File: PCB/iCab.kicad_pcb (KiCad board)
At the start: 2 copper layers, 58 parts, among them J1 Jack-DC, J10 PORT5, J11 V12, J2 Jack-DC, J3 PGM, J4 SERIAL, J5 PORT1, J6 PORT2, J7 OUT, J8 PORT3, J9 PORT4, Q1 IRFZ44, Q2 IRFZ44, Q3 IRFZ44, Q4 IRFZ44, Q5 IRFZ44, SW1 SW_Push, U1 Output, U2 PIC18F2550, U3 Output, Y1 Crystal

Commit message: new pcb
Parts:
- removed REF** (x2): MountingHole_2.2mm_M2, Mounting_Holes:MountingHole_2.2mm_M2
- added C10: 1µ, Capacitors_Tantalum_SMD:CP_Tantalum_Case-A_EIA-3216-18_Reflow, F.Cu at (97.8, 48.3)
- added C11: 10µ, Capacitors_THT:CP_Radial_D5.0mm_P2.00mm, F.Cu at (127.0, 53.3)
- added C12: 10µ, Capacitors_THT:CP_Radial_D5.0mm_P2.00mm, F.Cu at (127.0, 71.1)
- added C13: 10µ, Capacitors_THT:CP_Radial_D5.0mm_P2.00mm, F.Cu at (127.0, 88.9)
- added C14: 10µ, Capacitors_THT:CP_Radial_D5.0mm_P2.00mm, F.Cu at (127.0, 106.7)
- added C7: 10µ, Capacitors_THT:CP_Radial_D5.0mm_P2.00mm, F.Cu at (104.1, 47.0)
- added C8: 1µ, Capacitors_Tantalum_SMD:CP_Tantalum_Case-A_EIA-3216-18_Reflow, F.Cu at (85.1, 43.2)
- added C9: 10µ, Capacitors_THT:CP_Radial_D5.0mm_P2.00mm, F.Cu at (127.0, 35.6)
- added D10: D, Diodes_THT:D_T-1_P10.16mm_Horizontal, F.Cu at (92.7, 38.1)
- added D11: LED, LEDs:LED_0603_HandSoldering, F.Cu at (74.9, 52.7)
- added D12: LED, LEDs:LED_0603_HandSoldering, F.Cu at (74.9, 70.5)
- added D13: LED, LEDs:LED_0603_HandSoldering, F.Cu at (74.9, 88.3)
- added D14: LED, LEDs:LED_0603_HandSoldering, F.Cu at (74.9, 106.0)
- added D15: LED, LEDs:LED_0603_HandSoldering, F.Cu at (82.5, 113.0)
- added D16: LED, LEDs:LED_0603_HandSoldering, F.Cu at (116.8, 41.3)
- added D17: LED, LEDs:LED_0603_HandSoldering, F.Cu at (101.6, 79.4)
- added D18: LED, LEDs:LED_0603_HandSoldering, F.Cu at (116.8, 59.1)
- added D19: LED, LEDs:LED_0603_HandSoldering, F.Cu at (116.8, 76.8)
- added D20: LED, LEDs:LED_0603_HandSoldering, F.Cu at (116.8, 94.6)
- added D21: LED, LEDs:LED_0603_HandSoldering, F.Cu at (116.8, 112.4)
- added D8: D, Diodes_THT:D_T-1_P10.16mm_Horizontal, F.Cu at (114.3, 41.9)
- added D9: D, Diodes_THT:D_T-1_P10.16mm_Horizontal, F.Cu at (82.5, 34.3)
- added G***: LOGO, panda:LOGO3, F.Cu at (107.3, 55.9)
- added J12: D3, TerminalBlock_Phoenix:TerminalBlock_Phoenix_MKDS-1,5-2_1x02_P5.00mm_Horizontal, F.Cu at (128.3, 77.5)
- added J13: D4, TerminalBlock_Phoenix:TerminalBlock_Phoenix_MKDS-1,5-2_1x02_P5.00mm_Horizontal, F.Cu at (128.3, 95.2)
- added J14: D5, TerminalBlock_Phoenix:TerminalBlock_Phoenix_MKDS-1,5-2_1x02_P5.00mm_Horizontal, F.Cu at (128.3, 113.0)
- added R23: 511, Resistors_SMD:R_0603_HandSoldering, F.Cu at (78.1, 52.1)
- added R24: 511, Resistors_SMD:R_0603_HandSoldering, F.Cu at (78.1, 69.8)
- added R25: 511, Resistors_SMD:R_0603_HandSoldering, F.Cu at (78.1, 87.6)
- added R26: 511, Resistors_SMD:R_0603_HandSoldering, F.Cu at (78.1, 105.4)
- added R27: 511, Resistors_SMD:R_0603_HandSoldering, F.Cu at (82.5, 111.1)
- added R28: 1.2k, Resistors_SMD:R_0603_HandSoldering, F.Cu at (116.8, 45.7)
- added R29: 511, Resistors_SMD:R_0603_HandSoldering, F.Cu at (101.6, 83.8)
- added R30: 1.2k, Resistors_SMD:R_0603_HandSoldering, F.Cu at (116.8, 63.5)
- added R31: 1.2k, Resistors_SMD:R_0603_HandSoldering, F.Cu at (116.8, 81.3)
- added R32: 1.2k, Resistors_SMD:R_0603_HandSoldering, F.Cu at (116.8, 99.1)
- added R33: 1.2k, Resistors_SMD:R_0603_HandSoldering, F.Cu at (116.8, 116.8)
- added U4: L7805, TO_SOT_Packages_THT:TO-220_Vertical, F.Cu at (95.2, 43.2)
- C1: value 1µ -> 10µ; footprint Capacitors_Tantalum_SMD:CP_Tantalum_Case-A_EIA-3216-18_Reflow -> Capacitors_THT:CP_Radial_D5.0mm_P2.00mm
- C2: value 1n -> 10µ; footprint Capacitors_SMD:C_0603_HandSoldering -> Capacitors_THT:CP_Radial_D5.0mm_P2.00mm
- C4: value 100µ -> 10µ; footprint Capacitors_THT:CP_Radial_D10.0mm_P5.00mm -> Capacitors_THT:CP_Radial_D5.0mm_P2.00mm
- D1, D4, D5, D6, D7: footprint Diodes_SMD:D_MELF_Handsoldering -> Diodes_THT:D_T-1_P5.08mm_Horizontal
- J1: value Jack-DC -> S5; footprint Connectors:BARREL_JACK -> TerminalBlock_Phoenix:TerminalBlock_Phoenix_MKDS-1,5-2_1x02_P5.00mm_Horizontal
- J10: value PORT5 -> D1; footprint Pin_Headers:Pin_Header_Straight_1x05_Pitch2.54mm -> TerminalBlock_Phoenix:TerminalBlock_Phoenix_MKDS-1,5-2_1x02_P5.00mm_Horizontal
- J11: value V12 -> D2; footprint Pin_Headers:Pin_Header_Straight_1x05_Pitch2.54mm -> TerminalBlock_Phoenix:TerminalBlock_Phoenix_MKDS-1,5-2_1x02_P5.00mm_Horizontal
- J2: value Jack-DC -> S4; footprint Connectors:BARREL_JACK -> TerminalBlock_Phoenix:TerminalBlock_Phoenix_MKDS-1,5-2_1x02_P5.00mm_Horizontal
- J3: footprint Pin_Headers:Pin_Header_Angled_1x06_Pitch2.54mm -> Pin_Headers:Pin_Header_Straight_1x06_Pitch2.54mm
- J5: value PORT1 -> S3; footprint Pin_Headers:Pin_Header_Straight_1x05_Pitch2.54mm -> TerminalBlock_Phoenix:TerminalBlock_Phoenix_MKDS-1,5-2_1x02_P5.00mm_Horizontal
- J6: value PORT2 -> S2; footprint Pin_Headers:Pin_Header_Straight_1x05_Pitch2.54mm -> TerminalBlock_Phoenix:TerminalBlock_Phoenix_MKDS-1,5-2_1x02_P5.00mm_Horizontal
- J8: value PORT3 -> S1; footprint Pin_Headers:Pin_Header_Straight_1x05_Pitch2.54mm -> TerminalBlock_Phoenix:TerminalBlock_Phoenix_MKDS-1,5-2_1x02_P5.00mm_Horizontal
- J9: value PORT4 -> 12V; footprint Pin_Headers:Pin_Header_Straight_1x05_Pitch2.54mm -> TerminalBlock_Phoenix:TerminalBlock_Phoenix_MKDS-1,5-2_1x02_P5.00mm_Horizontal
- R21, R22: value 196 -> 511
- SW1: footprint Buttons_Switches_SMD:SW_SPST_KMR2 -> Buttons_Switches_THT:SW_PUSH_6mm
- moved J2 138.4 mm to (74.9, 100.3), turned to 90 degrees
- moved J7 108.7 mm to (111.8, 118.1), turned to 180 degrees
- moved J8 107.4 mm to (74.9, 47.0)
- moved D2 106.4 mm to (84.5, 118.1), turned to 270 degrees
- moved R20 105.9 mm to (88.3, 118.1)
- moved R22 105.8 mm to (86.4, 118.1)
- moved J1 105.4 mm to (74.9, 118.1), turned to 90 degrees
- moved R19 101.5 mm to (104.1, 118.1)
- moved J4 100.8 mm to (95.2, 118.1), turned to 180 degrees
- moved J9 97.3 mm to (106.7, 34.3), turned to 0 degrees
- moved R21 96.0 mm to (98.4, 118.1)
- moved R14 95.3 mm to (108.0, 115.6), turned to 180 degrees
- moved C4 94.8 mm to (99.1, 36.8), turned to 90 degrees
- moved R15 90.9 mm to (111.8, 115.6), turned to 0 degrees
- moved D3 89.6 mm to (100.3, 118.1), turned to 270 degrees
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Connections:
- C1 pad 1: +5V -> +12V
- C2 pad 1: +5V -> Net-(C2-Pad1)
- C4 pad 1: +12V -> Net-(C4-Pad1)
- C6 pad 1: +5V -> Net-(C4-Pad1)
- D1 pad 2: /PO1 -> Net-(D1-Pad2)
- D4 pad 2: /PO2 -> Net-(D4-Pad2)
- D5 pad 2: /PO3 -> Net-(D5-Pad2)
- D6 pad 2: /PO4 -> Net-(D6-Pad2)
- D7 pad 2: /PO5 -> Net-(D7-Pad2)
- J1 pad 1: +5V -> /SI5
- J10 pad 2: /PO5 -> Net-(D1-Pad2)
- J11 pad 2: +12V -> Net-(D4-Pad2)
- J2 pad 1: +12V -> /SI4
- J3 pad 6: /PGM -> (no net)
- J5 pad 1: +12V -> /SI3
- J5 pad 2: /PO1 -> GND
- J6 pad 1: +12V -> /SI2
- J6 pad 2: /PO2 -> GND
- J8 pad 1: +12V -> /SI1
- J8 pad 2: /PO3 -> GND
- J9 pad 2: /PO4 -> GND
- Q1 pad 2: /PO1 -> Net-(D1-Pad2)
- Q2 pad 2: /PO2 -> Net-(D4-Pad2)
- Q3 pad 2: /PO3 -> Net-(D5-Pad2)
- Q4 pad 2: /PO4 -> Net-(D6-Pad2)
- Q5 pad 2: /PO5 -> Net-(D7-Pad2)
- R1 pad 2: +5V -> +12V
- R10 pad 1: /SO4 -> /SO2
- R11 pad 1: /SO5 -> /SO1
- R2 pad 2: +5V -> +12V
- R3 pad 2: +5V -> +12V
- R5 pad 2: +5V -> +12V
- R6 pad 2: +5V -> +12V
- R7 pad 1: /SO1 -> /SO5
- R8 pad 1: /SO2 -> /SO4
- U1 pad 14: /SO5 -> /SO1
- U1 pad 15: /SO4 -> /SO2
- U1 pad 17: /SO2 -> /SO4
- U1 pad 18: /SO1 -> /SO5
- U2 pad 11: /L1 -> (no net)
- U2 pad 12: /L2 -> (no net)
- U2 pad 15: (no net) -> /L1
- U2 pad 16: (no net) -> /L2
- U2 pad 2: /SO1 -> (no net)
- U2 pad 26: /PGM -> Net-(R29-Pad2)
- U2 pad 3: /SO2 -> /SO1
- U2 pad 4: /SO3 -> /SO2
- U2 pad 5: /SO4 -> /SO3
- U2 pad 6: /SO5 -> /SO4
- U2 pad 7: (no net) -> /SO5
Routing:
- net +12V: track 136.5 -> 0.00 mm
- net /PO1: track 112.9 -> 0.00 mm
- net /PO2: track 92.0 -> 0.00 mm
- net /PO3: track 74.5 -> 0.00 mm
- net /SO5: track 11.5 -> 60.2 mm
- net /PO4: track 48.3 -> 0.00 mm
- net /SO4: track 11.5 -> 54.5 mm
- net /SO3: track 11.5 -> 48.3 mm
- net /P1: track 26.1 -> 56.5 mm
- net /L2: track 36.5 -> 6.13 mm
- net /SO2: track 11.5 -> 41.8 mm
- net /SI2: track 53.7 -> 23.8 mm
- net /SER_TX: track 45.8 -> 17.4 mm
- net /L1: track 32.8 -> 6.13 mm
- net /SI1: track 43.9 -> 17.4 mm, vias 1 -> 0
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- added copper zone on F.Cu, net +12V
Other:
- board outline added: 58.4 x 90.2 mm
- rule pad_to_mask_clearance: 0.2 -> 0
- rule trace_min: 0.2032 -> 0.2
- rule via_min_drill: 0.381 -> 0.3
- rule via_min_size: 0.508 -> 0.4

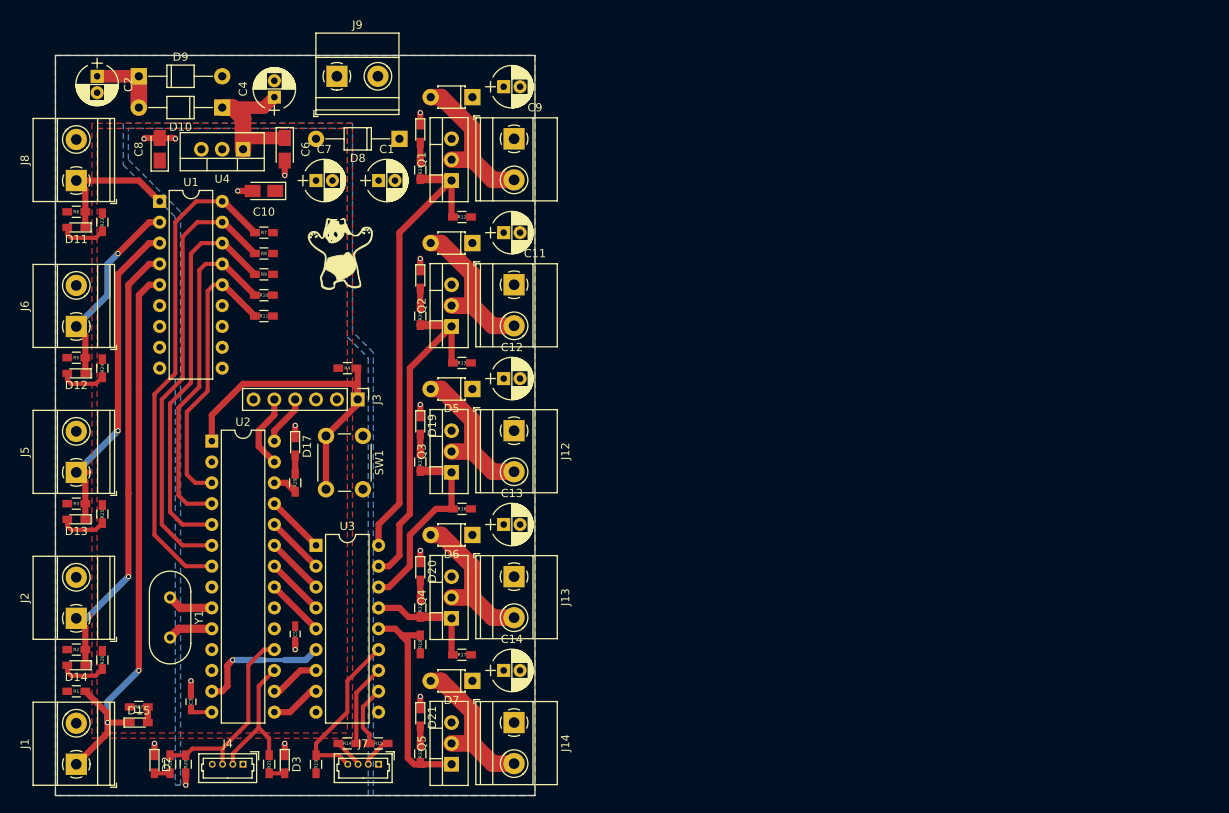
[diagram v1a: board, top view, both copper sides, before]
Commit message: update pcb references
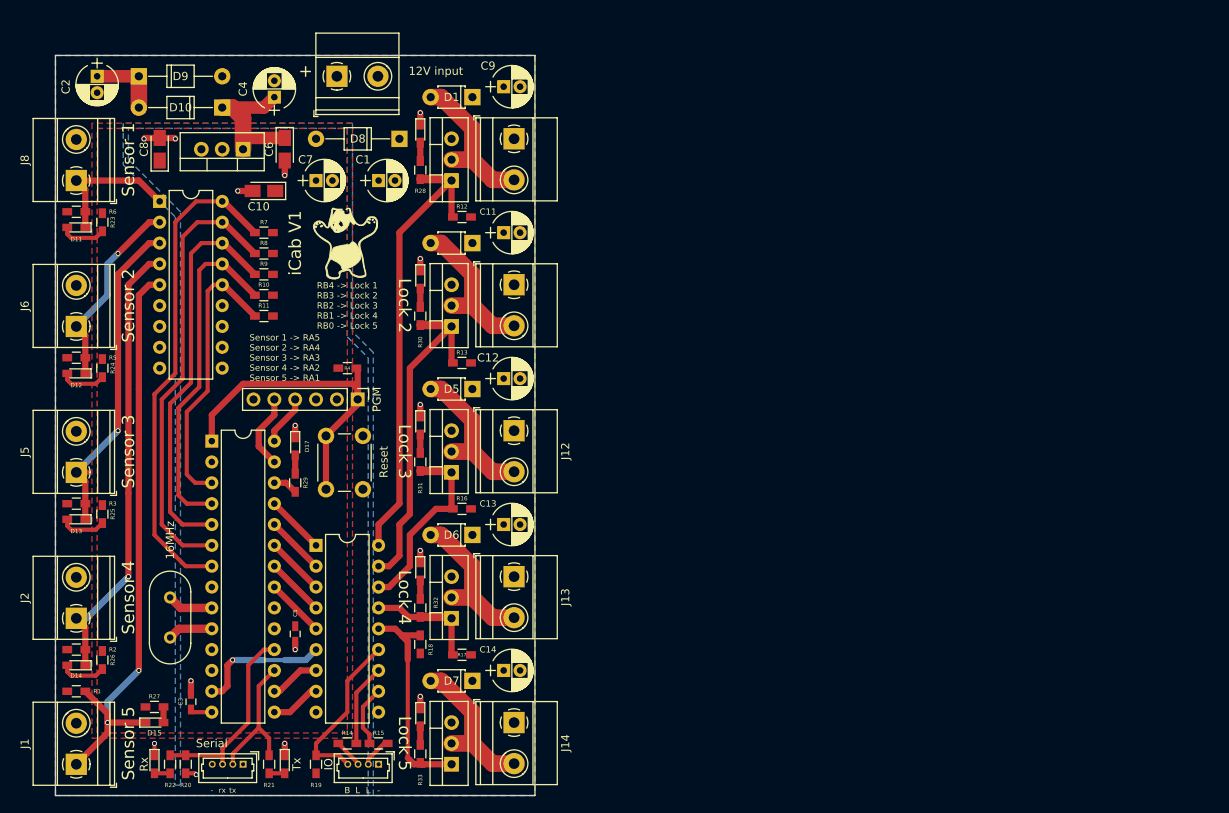
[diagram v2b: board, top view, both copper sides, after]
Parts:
- added G***: LOGO, KiCadLogos:galenus80_50, B.Cu at (101.6, 77.5)
- 12V input: renamed from J9
- moved D15 1.91 mm to (84.5, 113.0)
- moved R27 1.91 mm to (84.5, 111.1)
- moved G*** 1.42 mm to (108.0, 54.6)
- renumbered Y1 to 16MHz, J7 to IO, J3 to PGM, SW1 to Reset, D2 to Rx, J4 to Serial, D3 to Tx
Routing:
- net /SI5: track 71.0 -> 72.9 mm
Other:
- board text added: "+"
- board text added: "-"
- board text added: "B"
- board text added: "L"
- board text added: "Lock 2"
- board text added: "Lock 3"
- board text added: "Lock 4"
- board text added: "Lock 5"
- board text added: "RB4 -> Lock 1 RB3 -> Lock 2 RB2 -> Lock 3 RB1 -> Lock 4 RB0 -> Lock 5"
- board text added: "Sensor 1"
- board text added: "Sensor 1 -> RA5 Sensor 2 -> RA4 Sensor 3 -> RA3 Sensor 4 -> RA2 Sensor 5 -> RA1"
- board text added: "Sensor 2"
- board text added: "Sensor 3"
- board text added: "Sensor 4"
- board text added: "Sensor 5"
- board text added: "iCab V1"
- board text added: "rx"
- board text added: "tx"
